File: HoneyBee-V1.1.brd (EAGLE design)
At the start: 51.1 x 40.6 mm, 47 parts, among them IC2 CA3130EZLMP, Q1 2N5457

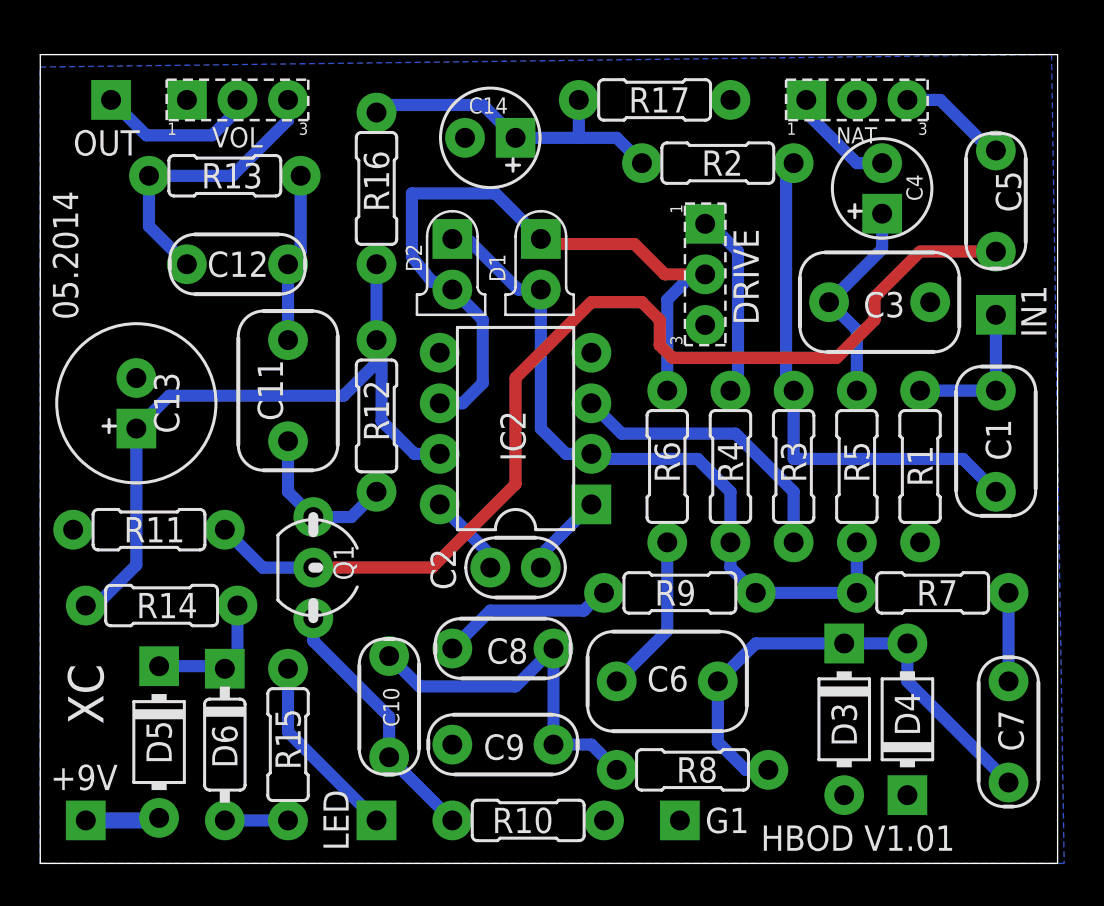
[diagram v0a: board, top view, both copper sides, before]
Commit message: Changes to layout and schematic.
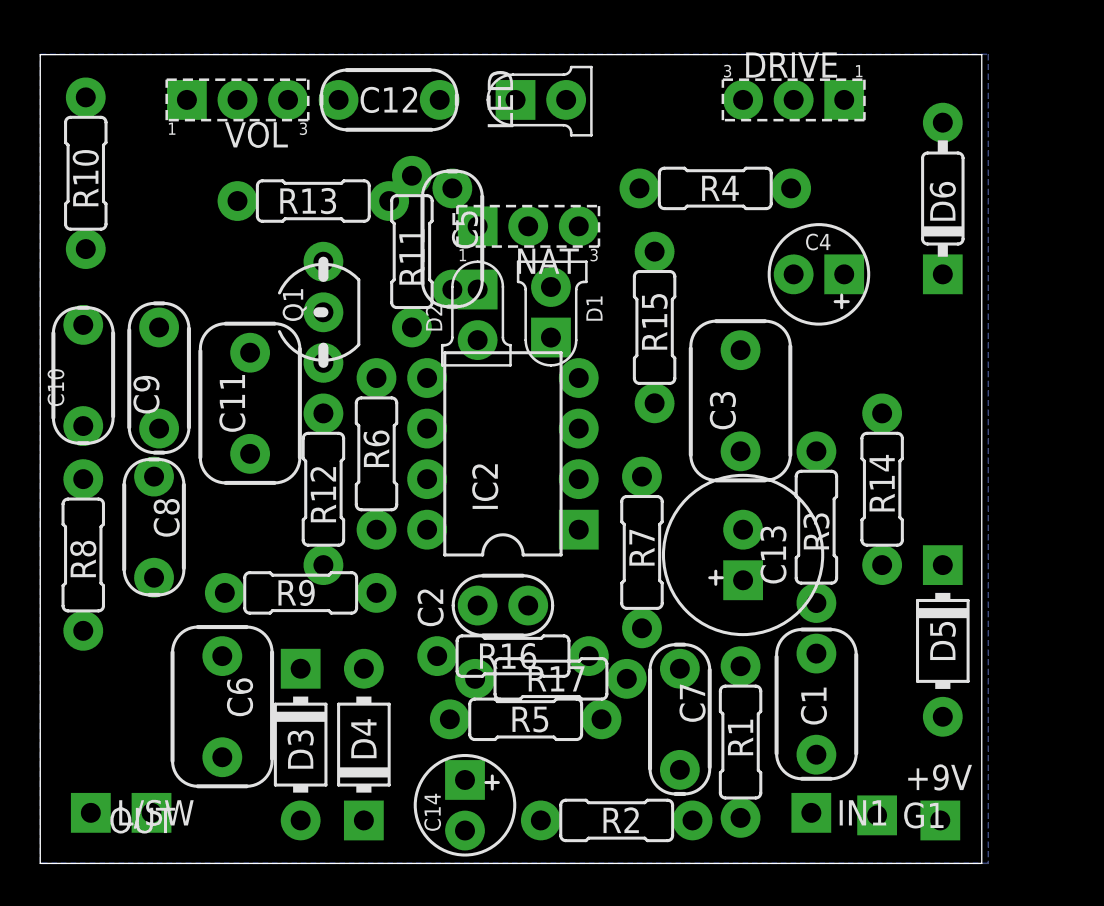
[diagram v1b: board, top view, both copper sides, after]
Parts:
- added L/SW: (no value), mb_supply:SQUARE
- LED: device mb_supply:SQUARE -> mb_diodes:LED3MM
- moved D6 45.3 mm to (45.3, 33.4), turned to 90 degrees
- moved +9V 42.9 mm to (45.2, 2.16)
- moved D5 39.7 mm to (45.3, 11.2)
- moved R10 39.4 mm to (2.29, 34.7), turned to 270 degrees
- moved LED 37.1 mm to (25.1, 38.4)
- moved R14 36.7 mm to (42.3, 18.8), turned to 90 degrees
- moved OUT 35.9 mm to (5.59, 2.54)
- moved C14 33.6 mm to (21.3, 2.92), turned to 270 degrees
- moved R2 33.4 mm to (29.0, 2.16)
- moved R8 32.5 mm to (2.16, 15.5), turned to 90 degrees
- moved C13 31.4 mm to (35.3, 15.5)
- moved R17 29.5 mm to (25.7, 9.27), turned to 0 degrees
- moved R15 27.9 mm to (30.9, 26.9)
- moved C5 27.4 mm to (20.7, 31.4)
- moved D3 27.3 mm to (13.1, 5.97)
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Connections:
- new net N$20: LED.A, R15.2
- net N$25: now also L/SW.1, LED.K; no longer LED.1, R15.2
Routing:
- net N$17: track 53.0 -> 0.00 mm
- net N$8: track 37.7 -> 0.00 mm
- net N$4: track 36.5 -> 0.00 mm
- net VC: track 36.4 -> 0.00 mm
- net N$1: track 26.0 -> 0.00 mm
- net N$12: track 25.6 -> 0.00 mm
- net N$14: track 18.2 -> 0.00 mm
- net N$19: track 16.9 -> 0.00 mm
- net N$2: track 14.5 -> 0.00 mm
- net N$22: track 14.4 -> 0.00 mm
- net N$16: track 13.1 -> 0.00 mm
- net N$3: track 10.6 -> 0.00 mm
- net N$25: track 9.46 -> 0.00 mm
- net N$9: track 9.37 -> 0.00 mm
- net N$15: track 8.78 -> 0.00 mm
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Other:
- board size 51.1 x 40.6 mm -> 47.3 x 40.6 mm
- board text removed: "05.2014"
- board text removed: "HBOD V1.01"
- board text removed: "XC"
